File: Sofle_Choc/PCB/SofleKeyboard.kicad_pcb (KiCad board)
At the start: 2 copper layers, 143.4 x 111.8 mm, 84 parts, among them J2 4PIN, J3 OLED, P1 i2c_pin, P2 i2c_pin, SW1 SW_PUSH_LED, SW10 SW_PUSH_LED, SW11 SW_PUSH_LED, SW12 SW_PUSH_LED, SW13 SW_PUSH_LED, SW14 SW_PUSH_LED, SW15 SW_PUSH_LED, SW16 SW_PUSH_LED, SW17 SW_PUSH_LED, SW18 SW_PUSH_LED, SW19 SW_PUSH_LED, SW2 SW_PUSH_LED, SW20 SW_PUSH_LED, SW21 SW_PUSH_LED, SW22 SW_PUSH_LED, SW23 SW_PUSH_LED, SW24 SW_PUSH_LED, SW25 Rotary_Encoder_Switch, SW26 SW_PUSH_LED, SW27 SW_PUSH_LED, SW28 SW_PUSH_LED, SW29 SW_PUSH_LED, SW3 SW_PUSH_LED, SW30 SW_PUSH_LED, SW4 SW_PUSH_LED, SW5 SW_PUSH_LED, SW6 SW_PUSH_LED, SW7 SW_PUSH_LED, SW8 SW_PUSH_LED, SW9 SW_PUSH_LED, U1 ProMicro

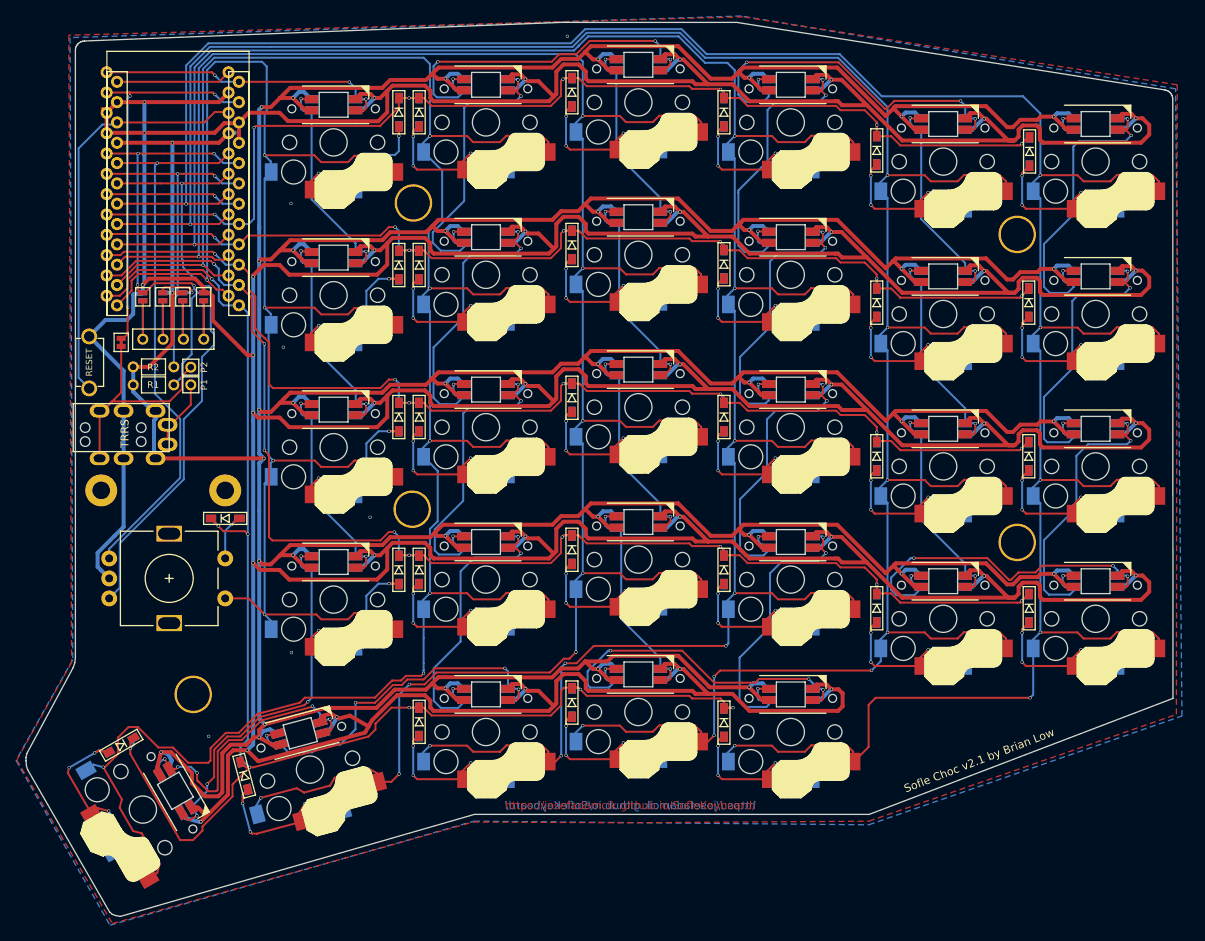
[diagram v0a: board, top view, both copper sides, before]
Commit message: add: parts for wireless support
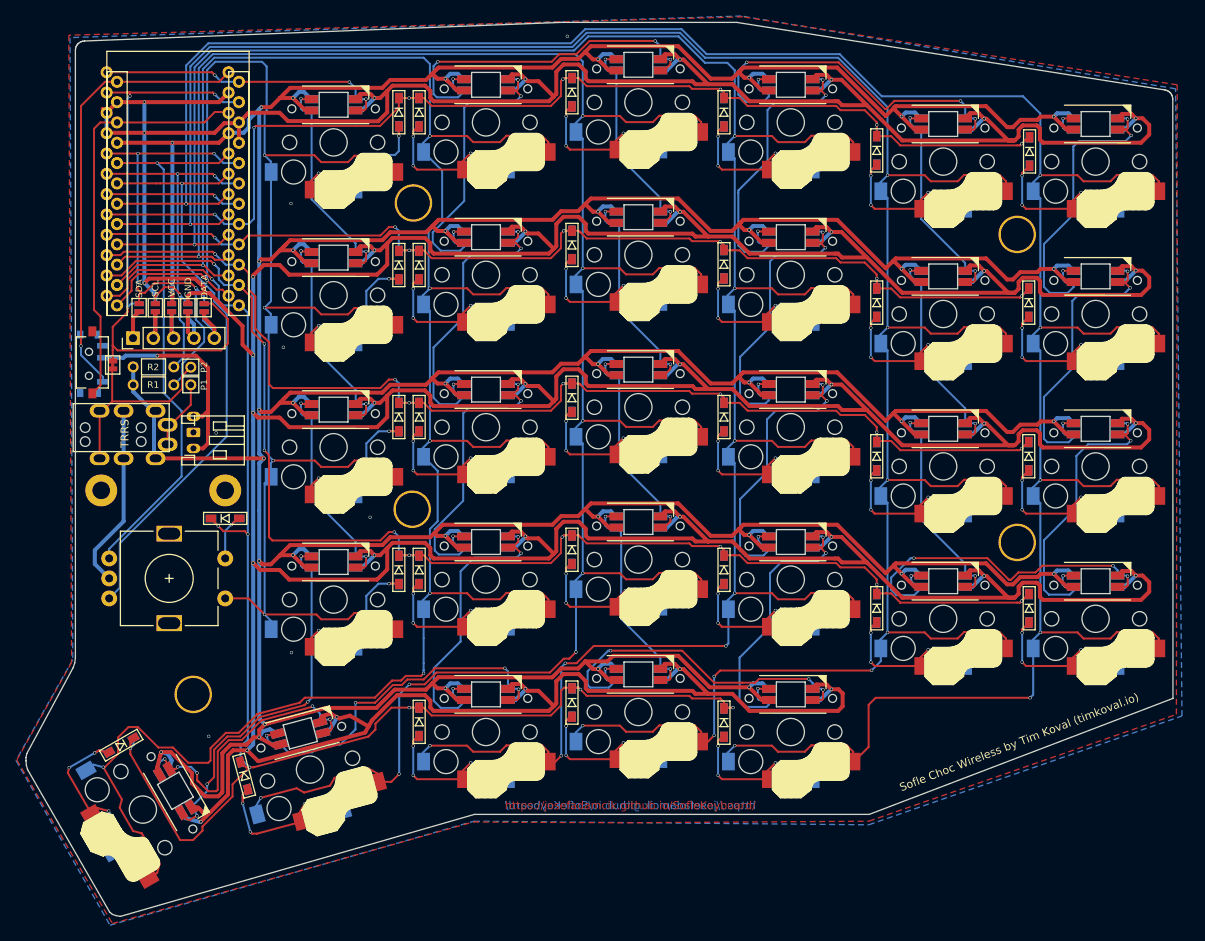
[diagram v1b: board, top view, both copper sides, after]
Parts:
- added J1: Conn_01x02, SofleChoc:JST_PH_S2B-PH-K_1x02_P2.00mm_DoubleSided, B.Cu at (102.9, 86.3)
- added JP1: DATA, SofleChoc:Jumper, F.Cu at (104.4, 70.7)
- added JP10: DATA, SofleChoc:Jumper, B.Cu at (96.2, 70.7)
- added SW31: SW_BATT1, Button_Switch_SMD:SW_SPDT_PCM12, B.Cu at (90.3, 77.7)
- J3: value OLED -> OLED_NiceVIew; footprint SofleKeyboard-footprint:OLED_4Pin -> Connector_PinHeader_2.54mm:PinHeader_1x05_P2.54mm_Vertical
- JP2: renamed from JP1; value Jumper_NO_Small -> GND
- JP3: renamed from JP2; value Jumper_NO_Small -> VCC
- JP4: renamed from JP3; value Jumper_NO_Small -> SCL
- JP5: renamed from JP4; value Jumper_NO_Small -> SDA
- JP6: renamed from JP5; value Jumper_NO_Small -> SDA
- JP7: renamed from JP6; value Jumper_NO_Small -> SCL
- JP8: renamed from JP7; value Jumper_NO_Small -> VCC
- JP9: renamed from JP8; value Jumper_NO_Small -> GND
- RSW1: footprint SofleKeyboard-footprint:TACT_SWITCH_TVBP06 -> Button_Switch_SMD:SW_Tactile_SPST_NO_Straight_CK_PTS636Sx25SMTRLFS
- moved W1 3.01 mm to (92.9, 77.8)
- moved JP2 2.39 mm to (102.3, 70.7)
- moved JP9 2.07 mm to (98.3, 70.6)
- moved JP3 1.95 mm to (100.3, 70.7)
- moved JP8 1.75 mm to (100.3, 70.7)
- moved JP4 1.65 mm to (98.3, 70.7)
- moved JP7 1.50 mm to (102.3, 70.7)
- moved JP5 1.43 mm to (96.2, 70.7)
- moved JP6 1.36 mm to (104.4, 70.7)
- moved J3 1.23 mm to (95.5, 74.5), turned to 90 degrees
- moved RSW1 0.40 mm to (90.4, 77.5)
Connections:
- J3 pad 1: Net-(J3-Pad1) -> Net-(J3-Pin_1)
- J3 pad 2: Net-(J3-Pad2) -> Net-(J3-Pin_2)
- J3 pad 3: Net-(J3-Pad3) -> Net-(J3-Pin_3)
- J3 pad 4: Net-(J3-Pad4) -> Net-(J3-Pin_4)
- JP2 pad 1: Net-(J3-Pad4) -> Net-(J3-Pin_4)
- JP3 pad 1: Net-(J3-Pad3) -> Net-(J3-Pin_3)
- JP4 pad 1: Net-(J3-Pad2) -> Net-(J3-Pin_2)
- JP5 pad 1: Net-(J3-Pad1) -> Net-(J3-Pin_1)
- JP6 pad 1: Net-(J3-Pad4) -> Net-(J3-Pin_5)
- JP7 pad 1: Net-(J3-Pad3) -> Net-(J3-Pin_4)
- JP8 pad 1: Net-(J3-Pad2) -> Net-(J3-Pin_3)
- JP9 pad 1: Net-(J3-Pad1) -> Net-(J3-Pin_2)
- SW6 pad 2: Net-(SW6-Pad2) -> unconnected-(SW6B-DOUT-Pad2)
- U1 pad 7: Net-(U1-Pad7) -> unconnected-(U1-D4(PD4)-Pad7)
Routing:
- net Net-(SW31-A): track 14.4 -> 55.8 mm, vias 0 -> 1
- net Net-(J1-Pin_2): track 0.00 -> 27.5 mm, vias 0 -> 1
- net DATA: track 48.7 -> 75.6 mm
- net Net-(U1-Pad7): track 17.0 -> 0.00 mm, vias 1 -> 0
- net unconnected-(U1-D4(PD4)-Pad7): track 0.00 -> 17.0 mm, vias 0 -> 1
- net GND: track 1090.4 -> 1073.5 mm, vias 43 -> 44
- net Net-(J3-Pad3): track 9.67 -> 0.00 mm
- net Net-(J3-Pad2): track 9.63 -> 0.00 mm
- net Net-(J3-Pad4): track 9.62 -> 0.00 mm
- net Net-(J3-Pad1): track 9.60 -> 0.00 mm
- net VCC: track 889.9 -> 882.1 mm
- net Net-(J3-Pin_5): track 0.00 -> 7.66 mm
- net Net-(J3-Pin_1): track 0.00 -> 7.49 mm
- net Net-(J3-Pin_4): track 0.00 -> 7.24 mm
- net Net-(J3-Pin_2): track 0.00 -> 6.83 mm
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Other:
- net class Default removed
- net class GND removed
- net class VCC removed
- board text added: "Sofle Choc Wireless by Tim Koval (timkoval.io)"
- board text removed: "Sofle Choc v2.1 by Brian Low"
